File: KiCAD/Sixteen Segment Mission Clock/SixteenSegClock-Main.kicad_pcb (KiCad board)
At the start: 2 copper layers, 114.3 x 165.1 mm, 54 parts, among them J1 Input, J2 Output, U1 L78S05CV

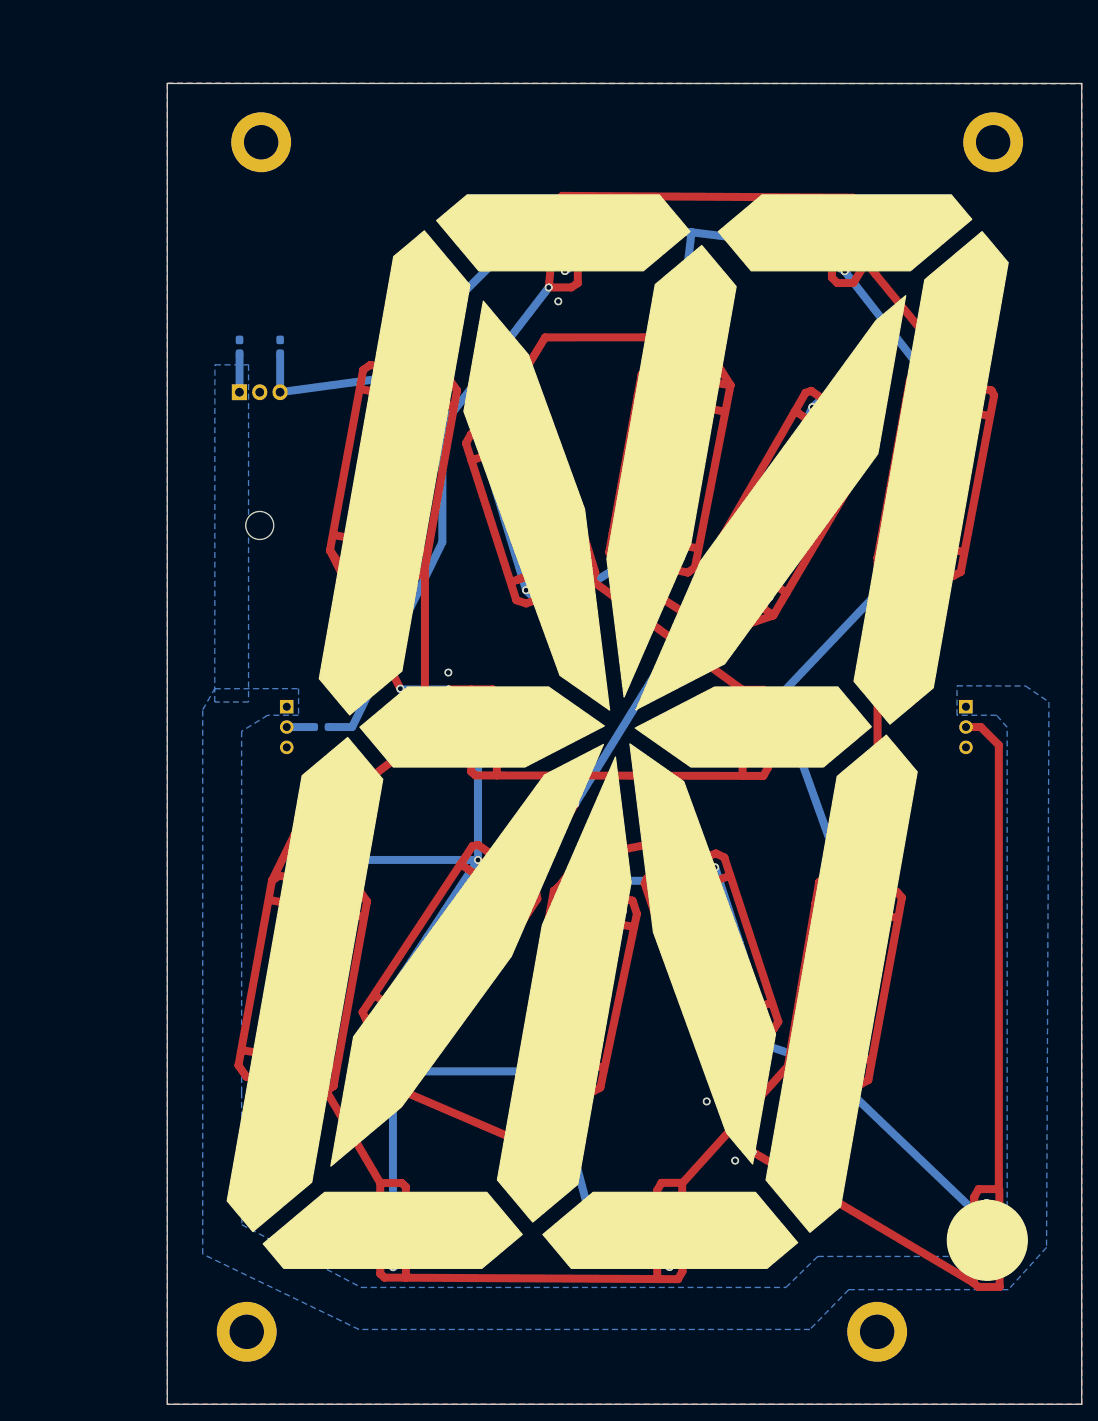
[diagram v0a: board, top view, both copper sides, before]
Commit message: Rounded corners
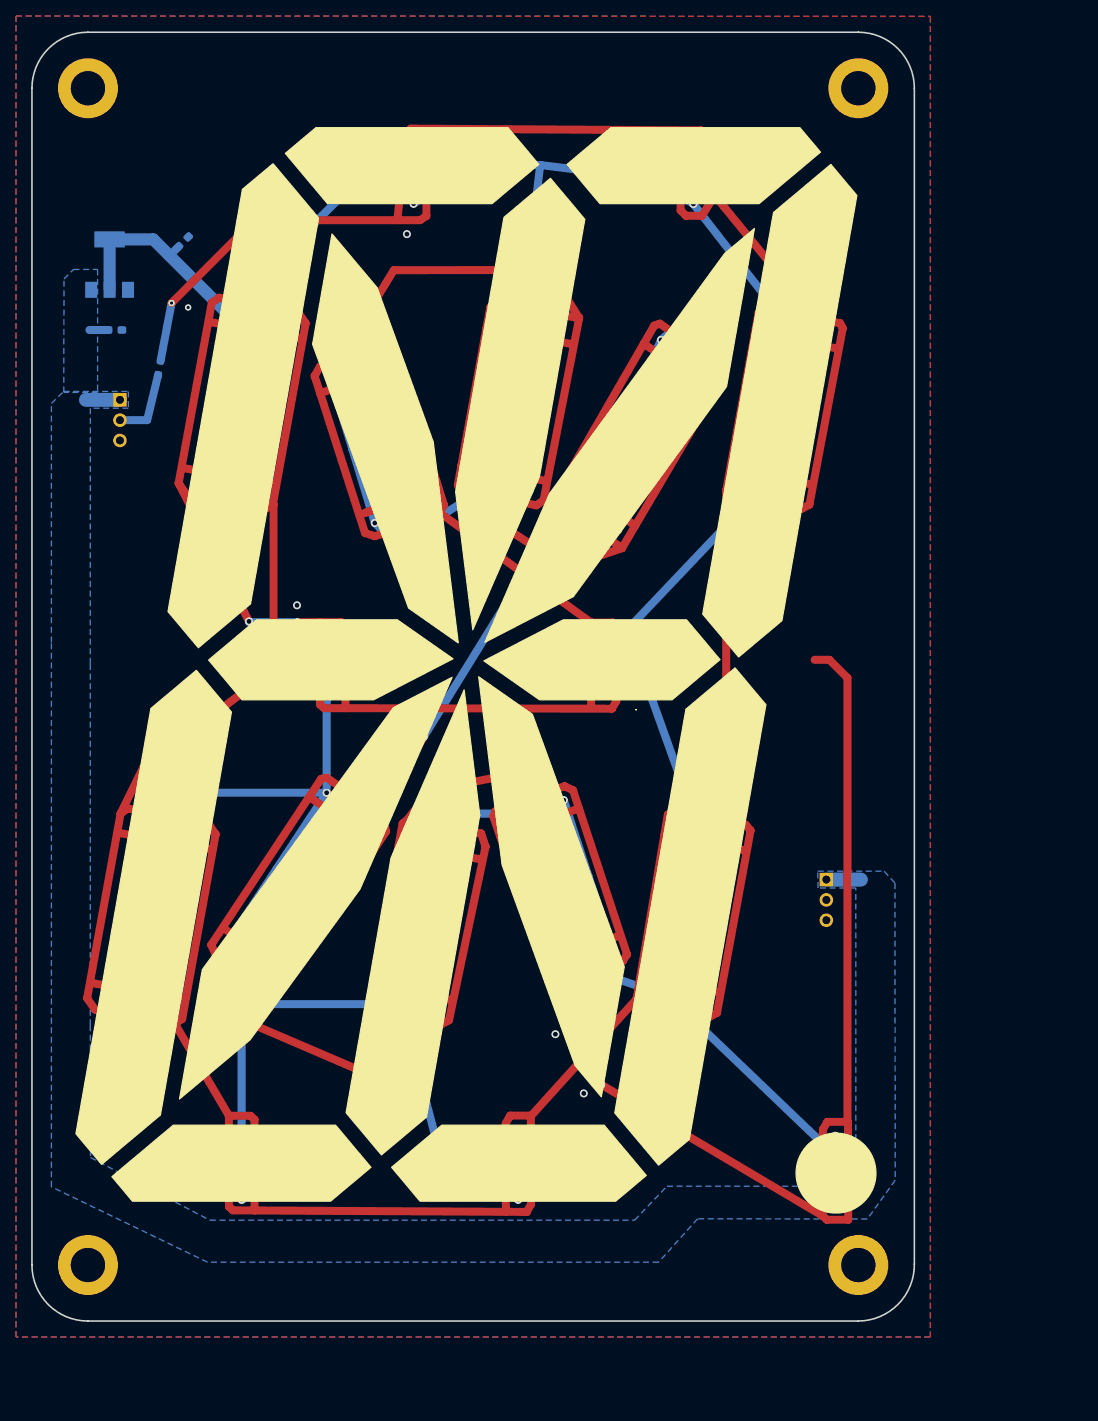
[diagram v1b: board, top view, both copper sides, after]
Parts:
- U1: value L78S05CV -> AZ1117-5.0; footprint Package_TO_SOT_THT:TO-220-3_Horizontal_TabDown -> Package_TO_SOT_SMD:SOT-223-3_TabPin2
- moved R1 49.3 mm to (37.9, 64.0), turned to 80 degrees
- moved J1 43.7 mm to (33.0, 68.0)
- moved J2 27.8 mm to (121.3, 133.0)
- moved U1 22.8 mm to (31.7, 51.0), turned to 90 degrees
- moved H4 22.7 mm to (29.0, 29.0)
- moved H2 21.5 mm to (29.0, 176.1)
- moved D15 20.7 mm to (104.2, 62.9)
- moved C3 20.7 mm to (74.7, 39.4)
- moved D18 20.7 mm to (83.7, 58.2)
- moved D8 20.7 mm to (72.7, 122.8)
- moved C10 20.7 mm to (46.9, 68.0)
- moved C16 20.7 mm to (54.7, 128.1)
- moved C8 20.7 mm to (53.3, 164.0)
- moved D21 20.7 mm to (35.5, 143.5)
- moved D24 20.7 mm to (50.6, 57.7)
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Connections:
- net /A1-A2 renamed /A1-A2L
- net /A2-B renamed /A2-BL
- net /B-C renamed /B-CL
- net /C-D2 renamed /C-D2L
- net /D1-E renamed /D1-EL
- net /D2-D1 renamed /D2-D1L
- net /E-F renamed /E-FL
- net /F-G1 renamed /F-G1L
- net /G1-G2 renamed /G1-G2L
- net /G2-H renamed /G2-HL
- net /H-I renamed /H-IR
- net /I-J renamed /I-JR
- net /J-K renamed /J-KR
- net /K-L renamed /K-LR
- net /L-M renamed /L-MR
- net /M-DP renamed /M-DPR
- U1 pad 1: /VIN_12V -> /GND
- U1 pad 2: /GND -> /V5_0
- U1 pad 3: /V5_0 -> /VIN_12V
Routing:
- net /DATA_IN: track 77.0 -> 51.8 mm
- net /V5_0: track 681.8 -> 691.0 mm
- net /VIN_12V: track 4.81 -> 10.9 mm
- net Net-(J1-Pin_2): track 3.41 -> 9.20 mm
- net /GND: vias 34 -> 35
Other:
- board size 114.3 x 165.1 mm -> 110.3 x 161.1 mm
